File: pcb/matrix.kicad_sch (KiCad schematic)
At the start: 129 parts

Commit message: add fn1
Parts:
- added D64: 1N4148, Diode_SMD:D_SOD-123, symbol Device:D
- added MX74: 1.25u, MX_Only:MXOnly-1.25U-NoLED, symbol Switch:SW_SPST
- D1, D10, D11, D12, D13, D14, D15, D16, D17, D18, D19, D2, D20, D21, D22, D23, D24, D25, D26, D27, D28, D29, D3, D30, D31, D32, D33, D34, D35, D36, D37, D38, D39, D4, D40, D41, D42, D43, D44, D45, D46, D47, D48, D49, D5, D50, D51, D52, D53, D54, D55, D56, D57, D58, D59, D6, D60, D61, D62, D63, D7, D8, D9: value (none) -> 1N4148; footprint (none) -> Diode_SMD:D_SOD-123
- MX1, MX10, MX11, MX12, MX13, MX14, MX15, MX18, MX19, MX2, MX20, MX21, MX22, MX23, MX24, MX25, MX26, MX27, MX28, MX29, MX3, MX33, MX34, MX35, MX36, MX37, MX38, MX39, MX4, MX40, MX41, MX42, MX43, MX46, MX47, MX48, MX49, MX5, MX50, MX51, MX52, MX53, MX54, MX55, MX57, MX6, MX68, MX7, MX72, MX8, MX9: value (none) -> 1u; footprint (none) -> MX_Only:MXOnly-1U-NoLED
- MX16: value (none) -> 2u; footprint (none) -> MX_Only:MXOnly-2U-NoLED
- MX17, MX30, MX67, MX71, MX73: value (none) -> 1.5u; footprint (none) -> MX_Only:MXOnly-1.5U-NoLED
- MX31, MX63, MX69: value (none) -> 1.25u; footprint (none) -> MX_Only:MXOnly-1.25U-NoLED
- MX32, MX56: value (none) -> 1.75u; footprint (none) -> MX_Only:MXOnly-1.75U-NoLED
- MX44, MX45: value (none) -> 2.25u; footprint (none) -> MX_Only:MXOnly-2.25U-NoLED
- MX58: value (none) -> 2.75u; footprint (none) -> MX_Only:MXOnly-2.75U-NoLED
- MX70: value (none) -> 2.75u; footprint (none) -> MX_Only:MXOnly-2.75U-ReversedStabilizers-NoLED
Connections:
- net COL4: now also MX74.2 (B)
- net ROW4: now also D64.1 (K)
- new net: D64.2 (A), MX74.1 (A)

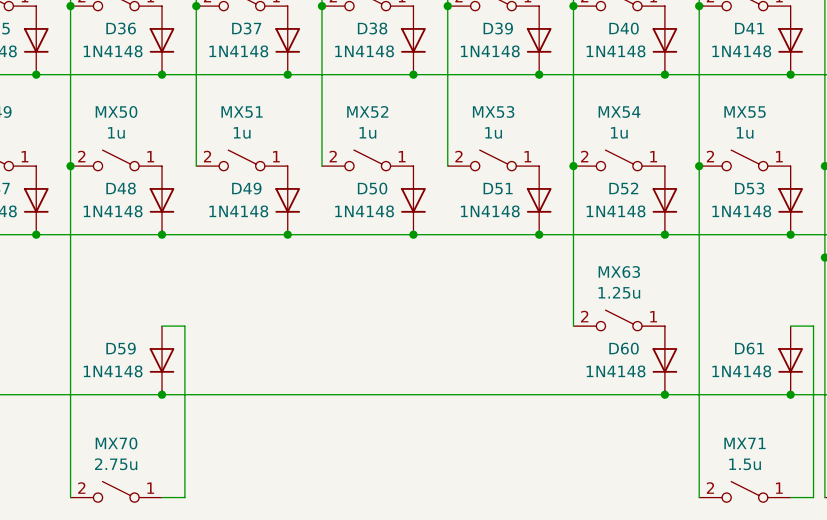
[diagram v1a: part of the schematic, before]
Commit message: bottom row done except for diodes wrong side
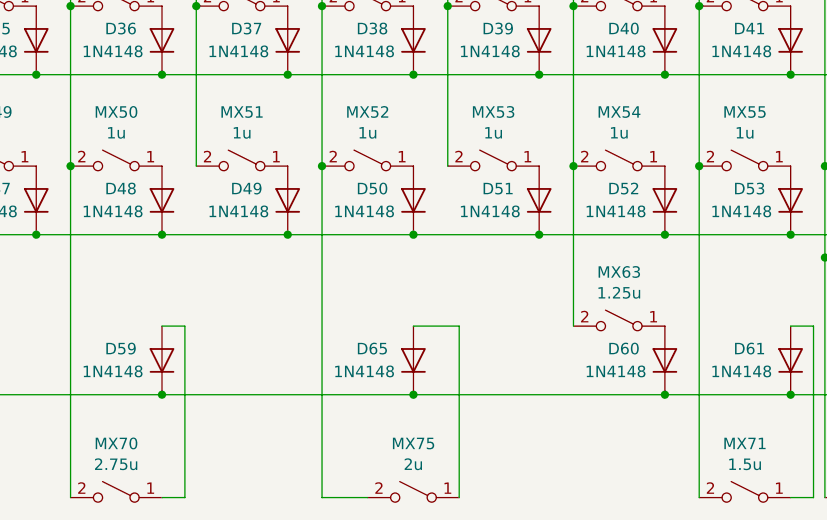
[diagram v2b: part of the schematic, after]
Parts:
- added D65: 1N4148, Diode_SMD:D_SOD-123, symbol Device:D
- added MX75: 2u, MX_Only:MXOnly-2U-ReversedStabilizers-NoLED, symbol Switch:SW_SPST
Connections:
- net COL8: now also MX75.2 (B)
- net ROW4: now also D65.1 (K)
- new net: D65.2 (A), MX75.1 (A)
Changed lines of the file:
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@@
   (junction (at 129.54 39.37) (diameter 0) (color 0 0 0 0)
   )
+  (junction (at 167.64 118.11) (diameter 0) (color 0 0 0 0)
+  )
   (junction (at 59.69 57.15) (diameter 0) (color 0 0 0 0)
   )
@@
   (junction (at 101.6 39.37) (diameter 0) (color 0 0 0 0)
   )
+  (junction (at 157.48 92.71) (diameter 0) (color 0 0 0 0)
+  )
   (junction (at 153.67 46.99) (diameter 0) (color 0 0 0 0)
   )
@@
     (stroke (width 0) (type default) (color 0 0 0 0))
   )
-  (wire (pts (xy 139.7 118.11) (xy 195.58 118.11))
+  (wire (pts (xy 139.7 118.11) (xy 167.64 118.11))
     (stroke (width 0) (type default) (color 0 0 0 0))
   )
@@
     (stroke (width 0) (type default) (color 0 0 0 0))
   )
+  (wire (pts (xy 172.72 129.54) (xy 172.72 110.49))
+    (stroke (width 0) (type default) (color 0 0 0 0))
+  )
   (wire (pts (xy 171.45 57.15) (xy 171.45 74.93))
     (stroke (width 0) (type default) (color 0 0 0 0))
@@
     (stroke (width 0) (type default) (color 0 0 0 0))
   )
+  (wire (pts (xy 172.72 110.49) (xy 167.64 110.49))
+    (stroke (width 0) (type default) (color 0 0 0 0))
+  )
   (wire (pts (xy 237.49 46.99) (xy 223.52 46.99))
     (stroke (width 0) (type default) (color 0 0 0 0))
@@
     (stroke (width 0) (type default) (color 0 0 0 0))
   )
+  (wire (pts (xy 157.48 92.71) (xy 157.48 129.54))
+    (stroke (width 0) (type default) (color 0 0 0 0))
+  )
   (wire (pts (xy 223.52 64.77) (xy 237.49 64.77))
     (stroke (width 0) (type default) (color 0 0 0 0))
@@
     (stroke (width 0) (type default) (color 0 0 0 0))
   )
+  (wire (pts (xy 167.64 118.11) (xy 195.58 118.11))
+    (stroke (width 0) (type default) (color 0 0 0 0))
+  )
   (wire (pts (xy 213.36 39.37) (xy 213.36 57.15))
     (stroke (width 0) (type default) (color 0 0 0 0))
@@
     (stroke (width 0) (type default) (color 0 0 0 0))
   )
+  (wire (pts (xy 157.48 129.54) (xy 162.56 129.54))
+    (stroke (width 0) (type default) (color 0 0 0 0))
+  )
   (wire (pts (xy 24.13 82.55) (xy 55.88 82.55))
     (stroke (width 0) (type default) (color 0 0 0 0))
@@
     (pin "2")
   )
+  (symbol (lib_id "Device:D") (at 167.64 114.3 90) (unit 1)
+    (in_bom yes) (on_board yes)
+    (property "Reference" "D65" (id 0) (at 161.29 113.03 90)
+      (effects (font (size 1.27 1.27)) (justify right))
+    )
+    (property "Value" "1N4148" (id 1) (at 158.75 115.57 90)
+      (effects (font (size 1.27 1.27)) (justify right))
+    )
+    (property "Footprint" "Diode_SMD:D_SOD-123" (id 2) (at 167.64 114.3 0)
+      (effects (font (size 1.27 1.27)) hide)
+    )
+    (property "Datasheet" "~" (id 3) (at 167.64 114.3 0)
+      (effects (font (size 1.27 1.27)) hide)
+    )
+    (property "LCSC Part #" "C81598" (id 4) (at 167.64 114.3 0)
+      (effects (font (size 1.27 1.27)) hide)
+    )
+    (pin "1")
+    (pin "2")
+  )
   (symbol (lib_id "Device:D") (at 111.76 114.3 90) (unit 1)
     (in_bom yes) (on_board yes)
@@
       (effects (font (size 1.27 1.27)) hide)
     )
+    (pin "1")
+    (pin "2")
+  )
+  (symbol (lib_id "Switch:SW_SPST") (at 167.64 129.54 0) (mirror y) (unit 1)
+    (in_bom yes) (on_board yes)
+    (property "Reference" "MX75" (id 0) (at 167.64 123.571 0))
+    (property "Value" "2u" (id 1) (at 167.64 125.8824 0))
+    (property "Footprint" "MX_Only:MXOnly-2U-ReversedStabilizers-NoLED" (id 2) (at 167.64 129.54 0)
+      (effects (font (size 1.27 1.27)) hide)
+    )
+    (property "Datasheet" "~" (id 3) (at 167.64 129.54 0)
+      (effects (font (size 1.27 1.27)) hide)
+    )

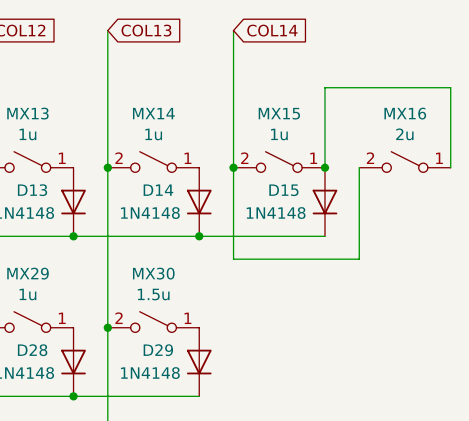
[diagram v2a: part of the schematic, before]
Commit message: remove 2u bs option due to leaf spring interference
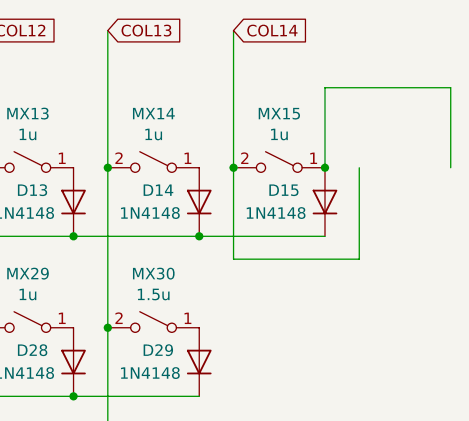
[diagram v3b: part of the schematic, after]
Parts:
- removed MX16: 2u, MX_Only:MXOnly-2U-NoLED, symbol Switch:SW_SPST
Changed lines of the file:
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@@
-    (pin "2")
-  )
-  (symbol (lib_id "Switch:SW_SPST") (at 260.35 39.37 0) (mirror y) (unit 1)
-    (in_bom yes) (on_board yes)
-    (property "Reference" "MX16" (id 0) (at 260.35 33.401 0))
-    (property "Value" "2u" (id 1) (at 260.35 35.7124 0))
-    (property "Footprint" "MX_Only:MXOnly-2U-NoLED" (id 2) (at 260.35 39.37 0)
-      (effects (font (size 1.27 1.27)) hide)
-    )
-    (property "Datasheet" "~" (id 3) (at 260.35 39.37 0)
-      (effects (font (size 1.27 1.27)) hide)
-    )
-    (pin "1")
     (pin "2")
   )

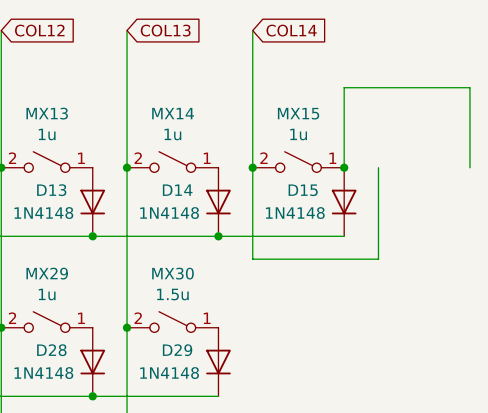
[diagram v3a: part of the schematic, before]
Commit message: pass drc checks
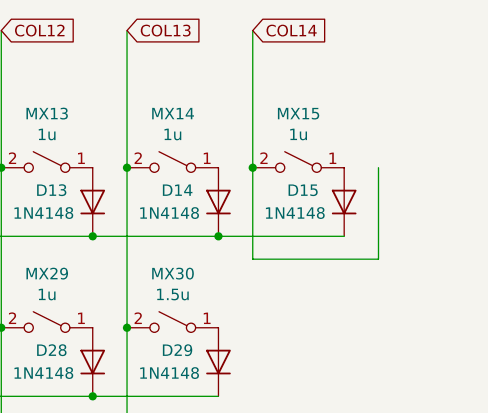
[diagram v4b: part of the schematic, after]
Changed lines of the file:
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@@
   (junction (at 195.58 46.99) (diameter 0) (color 0 0 0 0)
   )
-  (junction (at 251.46 39.37) (diameter 0) (color 0 0 0 0)
-  )
   (junction (at 87.63 57.15) (diameter 0) (color 0 0 0 0)
   )
@@
     (stroke (width 0) (type default) (color 0 0 0 0))
   )
-  (wire (pts (xy 265.43 30.48) (xy 251.46 30.48))
-    (stroke (width 0) (type default) (color 0 0 0 0))
-  )
   (wire (pts (xy 251.46 92.71) (xy 251.46 83.82))
     (stroke (width 0) (type default) (color 0 0 0 0))
@@
     (stroke (width 0) (type default) (color 0 0 0 0))
   )
-  (wire (pts (xy 251.46 30.48) (xy 251.46 39.37))
-    (stroke (width 0) (type default) (color 0 0 0 0))
-  )
   (wire (pts (xy 73.66 24.13) (xy 73.66 39.37))
     (stroke (width 0) (type default) (color 0 0 0 0))
@@
     (stroke (width 0) (type default) (color 0 0 0 0))
   )
-  (wire (pts (xy 265.43 39.37) (xy 265.43 30.48))
-    (stroke (width 0) (type default) (color 0 0 0 0))
-  )
